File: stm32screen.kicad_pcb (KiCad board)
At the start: 4 copper layers, 46 x 46 mm, 36 parts, among them J1 SWD, J2 GC9A01, J3 OIL, J4 OIL PRESS, J5 POWER IN, J6 EGT, SW2 SW_Push, U1 TS1117BCW-3.3, U2 STM32F407VETx, U3 MAX31856

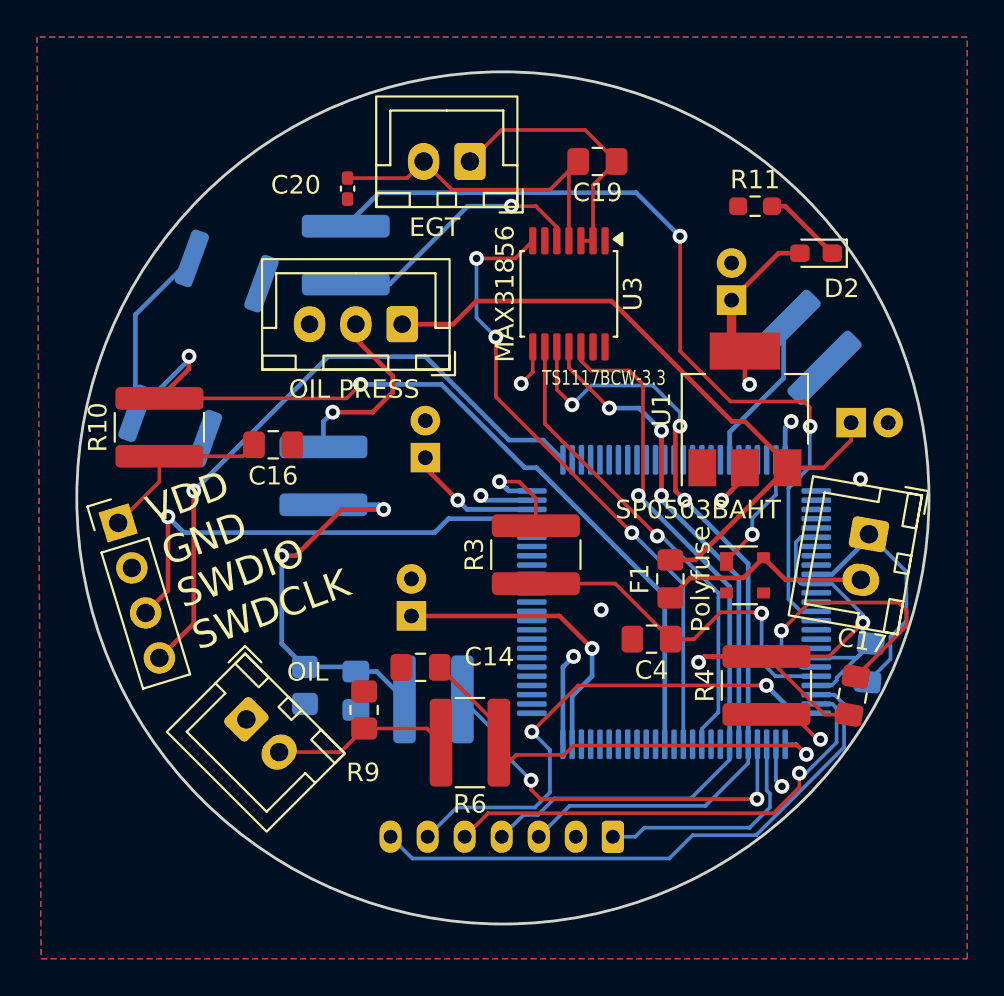
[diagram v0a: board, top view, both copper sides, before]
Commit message: Small trace changes
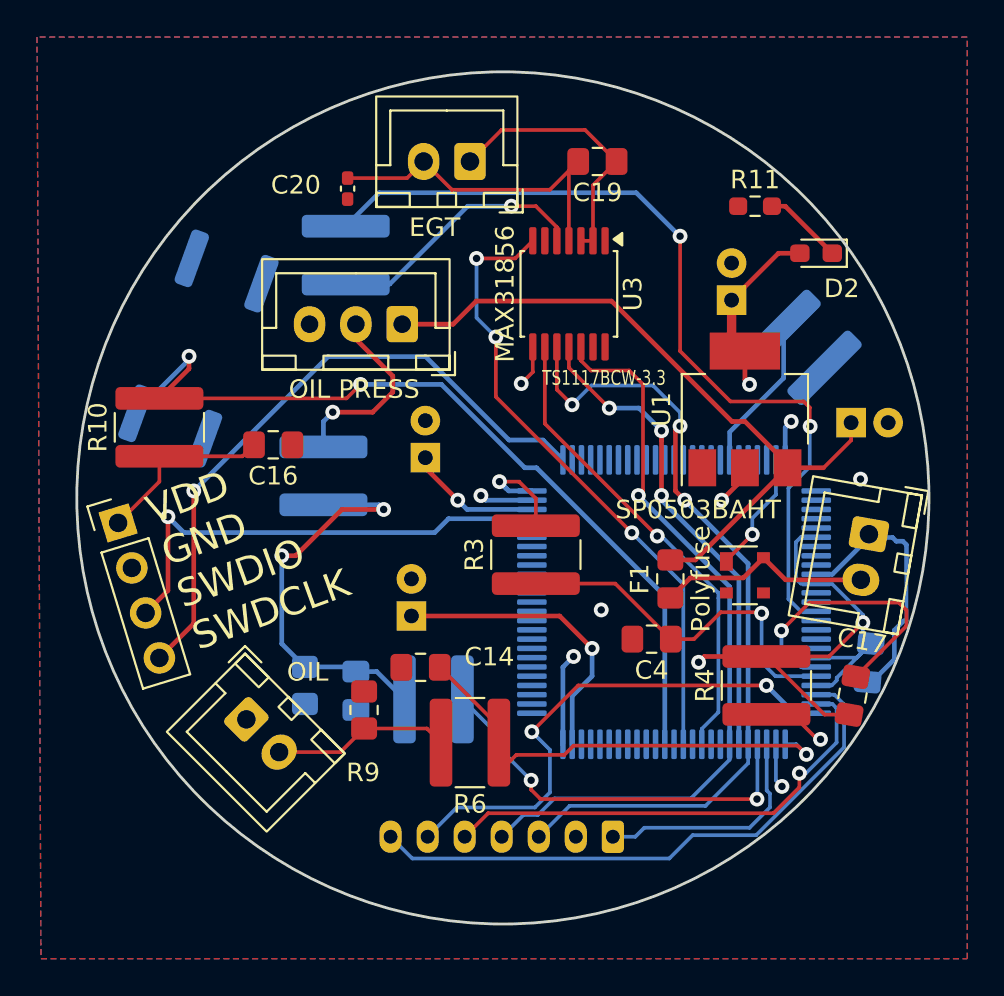
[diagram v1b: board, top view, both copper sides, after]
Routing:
- net Net-(U2-PE8): track 57.2 -> 47.5 mm
- net GND: track 41.2 -> 42.3 mm
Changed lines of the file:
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@@
 		(fp_line
 			(start -0.261252 0.734999)
-			(end 0.261251 0.734999)
+			(end 0.261251 0.734998)
 			(stroke
 				(width 0.12)
@@
 		)
 		(fp_line
-			(start -0.261251 -0.734999)
+			(start -0.261251 -0.734998)
 			(end 0.261252 -0.734999)
 			(stroke
@@
 		(tags "CK C&K SPST")
 		(property "Reference" "SW2"
-			(at -0.241564 4.279501 70)
+			(at -0.241563 4.279501 70)
 			(layer "B.SilkS")
 			(effects
@@
 		(fp_line
 			(start -0.261252 -0.735)
-			(end 0.261252 -0.734998)
+			(end 0.261252 -0.734997)
 			(stroke
 				(width 0.12)
@@
 		)
 		(fp_line
-			(start -0.261252 0.734998)
+			(start -0.261252 0.734997)
 			(end 0.261252 0.735)
 			(stroke
@@
 	)
 	(segment
-		(start 137.675 86.875)
-		(end 138 87.2)
-		(width 0.2)
+		(start 142.8496 81.5594)
+		(end 142.621 81.5594)
+		(width 0.25)
 		(layer "B.Cu")
 		(net 2)
 	)
 	(segment
-		(start 142.621 81.5594)
-		(end 143.85665 80.32375)
+		(start 137.675 86.875)
+		(end 138 87.2)
 		(width 0.2)
 		(layer "B.Cu")
@@
 	)
 	(segment
+		(start 143.9672 73.7616)
+		(end 142.869329 73.7616)
+		(width 0.25)
+		(layer "B.Cu")
+		(net 2)
+	)
+	(segment
 		(start 142.911576 81.678552)
 		(end 143.044952 81.678552)
@@
 	)
 	(segment
+		(start 142.869329 73.7616)
+		(end 142.694684 73.586955)
+		(width 0.25)
+		(layer "B.Cu")
+		(net 2)
+	)
+	(segment
+		(start 144.0688 78.7654)
+		(end 144.0688 80.3402)
+		(width 0.25)
+		(layer "B.Cu")
+		(net 2)
+	)
+	(segment
+		(start 144.719 74.1578)
+		(end 144.526 73.9648)
+		(width 0.25)
+		(layer "B.Cu")
+		(net 2)
+	)
+	(segment
+		(start 144.0688 80.3402)
+		(end 142.8496 81.5594)
+		(width 0.25)
+		(layer "B.Cu")
+		(net 2)
+	)
+	(segment
 		(start 142.694684 73.774494)
 		(end 142.694684 73.586955)
@@
 	(segment
 		(start 144.719 78.268364)
-		(end 144.719 75.611271)
-		(width 0.2)
+		(end 144.565836 78.268364)
+		(width 0.25)
 		(layer "B.Cu")
 		(net 2)
 	)
 	(segment
-		(start 143.85665 79.130714)
-		(end 144.719 78.268364)
-		(width 0.2)
+		(start 144.526 73.9648)
+		(end 144.1704 73.9648)
+		(width 0.25)
 		(layer "B.Cu")
 		(net 2)
 	)
 	(segment
-		(start 144.719 75.611271)
-		(end 142.694684 73.586955)
+		(start 144.719 78.268364)
+		(end 144.719 75.611271)
 		(width 0.2)
 		(layer "B.Cu")
@@
 	)
 	(segment
-		(start 143.85665 80.32375)
-		(end 143.85665 79.130714)
-		(width 0.2)
+		(start 144.1704 73.9648)
+		(end 143.9672 73.7616)
+		(width 0.25)
 		(layer "B.Cu")
 		(net 2)
@@
 	)
 	(segment
+		(start 144.565836 78.268364)
+		(end 144.0688 78.7654)
+		(width 0.25)
+		(layer "B.Cu")
+		(net 2)
+	)
+	(segment
 		(start 136.4 72.722709)
 		(end 136.4 73.6)
@@
 	)
 	(segment
+		(start 144.719 75.611271)
+		(end 144.719 74.1578)
+		(width 0.25)
+		(layer "B.Cu")
+		(net 2)
+	)
+	(segment
 		(start 126 78)
 		(end 118 78)
@@
 		(width 0.25)
 		(layer "B.Cu")
-		(net 20)
-	)
-	(segment
-		(start 103.099029 61.740235)
-		(end 106.143008 58.696256)
-		(width 0.25)
-		(layer "B.Cu")
-		(net 20)
-	)
-	(segment
-		(start 103.099029 67.05952)
-		(end 103.099029 61.740235)
-		(width 0.25)
-		(layer "B.Cu")

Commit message: A bit neater layout. Add missing parts to PCB. Refine silkscreen. New screenshots
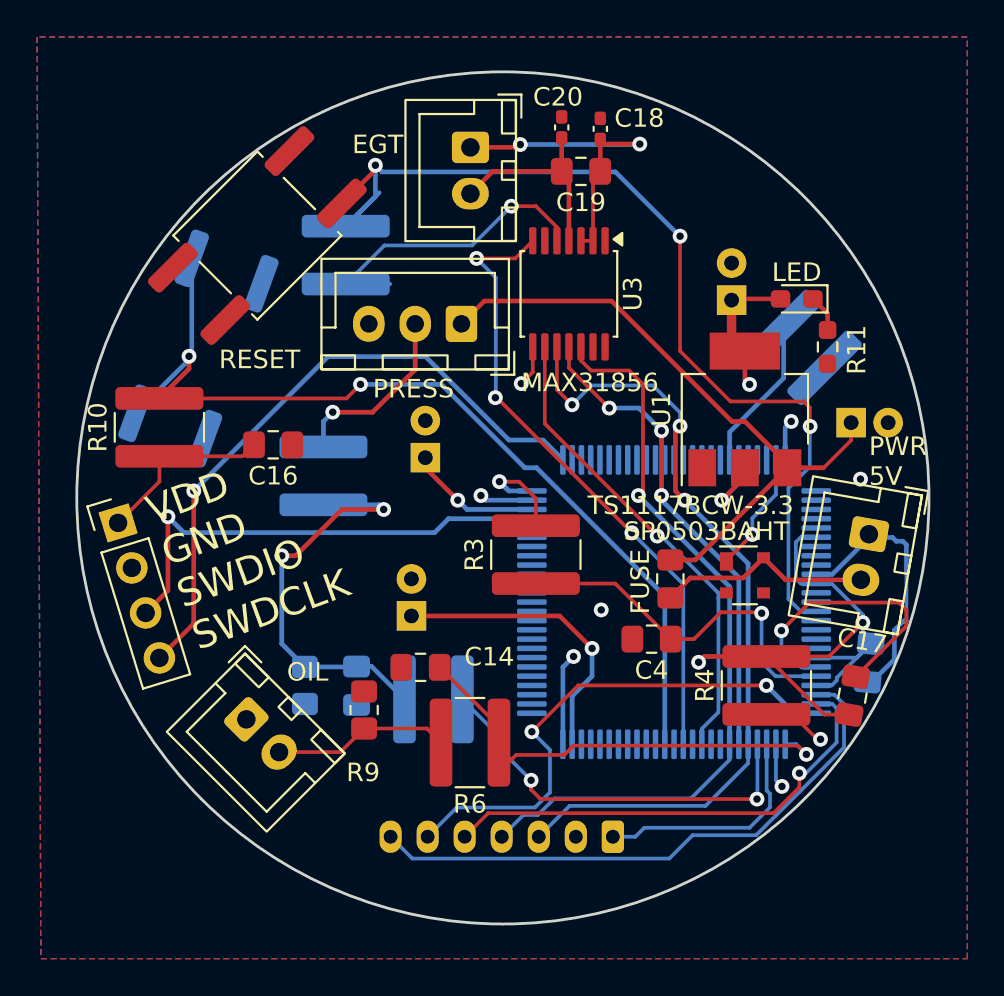
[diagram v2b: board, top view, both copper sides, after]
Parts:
- added C18: 0.01uF, Capacitor_SMD:C_0402_1005Metric_Pad0.74x0.62mm_HandSolder, F.Cu at (128.2, 51.7)
- added RESET: SW_Push, Button_Switch_SMD:SW_Push_1P1T_NO_CK_KSC9xxG, F.Cu at (109.7, 57.5)
- F1: value Polyfuse -> FUSE
- J4: value OIL PRESS -> PRESS
- moved C20 12.0 mm to (126.1, 51.6), turned to 90 degrees
- moved R11 8.55 mm to (140.5, 63.5), turned to 90 degrees
- moved J4 3.20 mm to (120.7, 62.2)
- moved D2 2.68 mm to (138.8, 60.9)
- moved C19 1.04 mm to (127.1, 54.0)
- moved J6 0.76 mm to (121.2, 52.7), turned to -90 degrees
- moved C15 0.27 mm to (115.0, 81.8)
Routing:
- net NRST: track 46.8 -> 54.3 mm, vias 2 -> 3
- net Net-(J6-Pin_2): track 18.6 -> 11.1 mm
- net Net-(U2-PE8): track 47.5 -> 52.9 mm
- net Vin: track 38.5 -> 35.3 mm
- net Net-(J6-Pin_1): track 14.8 -> 17.7 mm, vias 0 -> 2
- net Net-(D2-K): track 4.31 -> 2.01 mm
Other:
- board text added: "PWR 5V"

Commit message: THT caps to MLCC as per TS1117B datasheet. STM32 ref caps as well
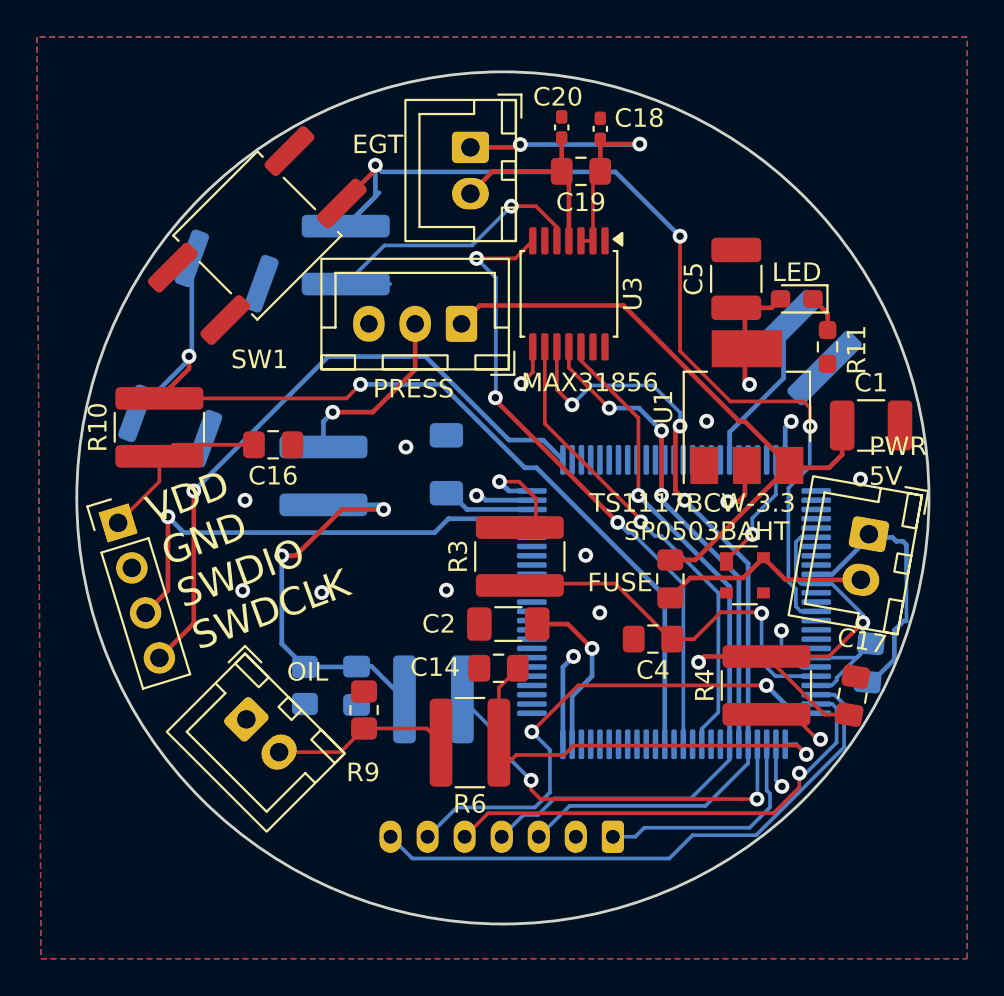
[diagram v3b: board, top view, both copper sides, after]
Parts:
- C1: footprint Capacitor_THT:CP_Radial_D5.0mm_P2.00mm -> Capacitor_SMD:C_1210_3225Metric_Pad1.33x2.70mm_HandSolder; moved to F.Cu
- C2: footprint Capacitor_THT:CP_Radial_D5.0mm_P2.00mm -> Capacitor_SMD:C_1206_3216Metric_Pad1.33x1.80mm_HandSolder; moved to F.Cu
- C3: footprint Capacitor_THT:CP_Radial_D5.0mm_P2.00mm -> Capacitor_SMD:C_1206_3216Metric_Pad1.33x1.80mm_HandSolder
- C5: value 10uF -> 100uF; footprint Capacitor_THT:CP_Radial_D5.0mm_P2.00mm -> Capacitor_SMD:C_1210_3225Metric_Pad1.33x2.70mm_HandSolder; moved to F.Cu
- moved C2 5.25 mm to (123.2, 78.4), turned to 180 degrees
- moved C14 4.21 mm to (122.7, 80.8)
- moved C3 1.19 mm to (119.9, 69.8)
- moved C5 1.17 mm to (135.5, 59.8)
- moved C1 1.09 mm to (142.8, 67.7)
- moved R3 0.87 mm to (123.9, 74.8)
- moved U1 0.16 mm to (136.1, 66.7)
- moved C4 0.07 mm to (131.0, 79.2)
- renumbered RESET to SW1
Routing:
- net GND: track 42.3 -> 30.0 mm, vias 6 -> 13
- net Net-(U2-VCAP_1): track 16.1 -> 9.12 mm
- net Net-(U2-VCAP_2): track 7.23 -> 4.21 mm, vias 1 -> 0
- net SDI: track 41.0 -> 39.6 mm
- net VDD: track 100.7 -> 101.9 mm
- net Net-(U2-PA3): track 25.2 -> 24.2 mm

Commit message: Adjusted silkscreen and component layout, changed some component values so that silkscreen doesn't change every time
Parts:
- SW1: value SW_Push -> NRST
- SW2: value SW_Push -> USER
- moved C1 1.00 mm to (142.6, 66.8)
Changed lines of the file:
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@@
 	(footprint "Capacitor_SMD:C_1210_3225Metric_Pad1.33x2.70mm_HandSolder"
 		(layer "F.Cu")
-		(at 142.8111 67.7164)
+		(at 142.5571 66.7512)
 		(descr "Capacitor SMD 1210 (3225 Metric), square (rectangular) end terminal, IPC-7351 nominal with elongated pad for handsoldering. (Body size source: IPC-SM-782 page 76, https://www.pcb-3d.com/wordpress/wp-content/uploads/ipc-sm-782a_amendment_1_and_2.pdf), generated with kicad-footprint-generator")
 		(tags "capacitor handsolder")
@@
 			(at -4.647566 4.8198 0)
 			(layer "F.SilkS")
+			(hide yes)
 			(effects
 				(font
@@
 			)
 		)
-		(property "Value" "SW_Push"
-			(at 0 -4.23 45)
-			(layer "F.Fab")
+		(property "Value" "NRST"
+			(at -3.480133 4.191182 45)
+			(layer "F.SilkS")
 			(effects
 				(font
@@
 		(tags "resistor handsolder")
 		(property "Reference" "R11"
-			(at -0.1543 1.5748 270)
+			(at 0.8909 2.1844 0)
 			(layer "F.SilkS")
 			(effects
@@
 		(tags "resistor handsolder")
 		(property "Reference" "R5"
-			(at -3.0125 3.32 0)
+			(at 0.0107 3.3536 0)
 			(layer "B.SilkS")
 			(effects
@@
 		(tags "resistor handsolder")
 		(property "Reference" "R7"
-			(at 2.794 -0.254 0)
+			(at -2.502 -0.018 0)
 			(layer "B.SilkS")
 			(effects
@@
 		(tags "capacitor handsolder")
 		(property "Reference" "C15"
-			(at 4.4495 1.3858 180)
+			(at -2.6201 0.0254 180)
 			(layer "B.SilkS")
 			(effects
@@
 			(at -0.241563 4.279501 70)
 			(layer "B.SilkS")
+			(hide yes)
 			(effects
 				(font
@@
 			)
 		)
-		(property "Value" "SW_Push"
+		(property "Value" "USER"
 			(at 0 4.23 70)
-			(layer "B.Fab")
+			(layer "B.SilkS")
 			(effects
 				(font

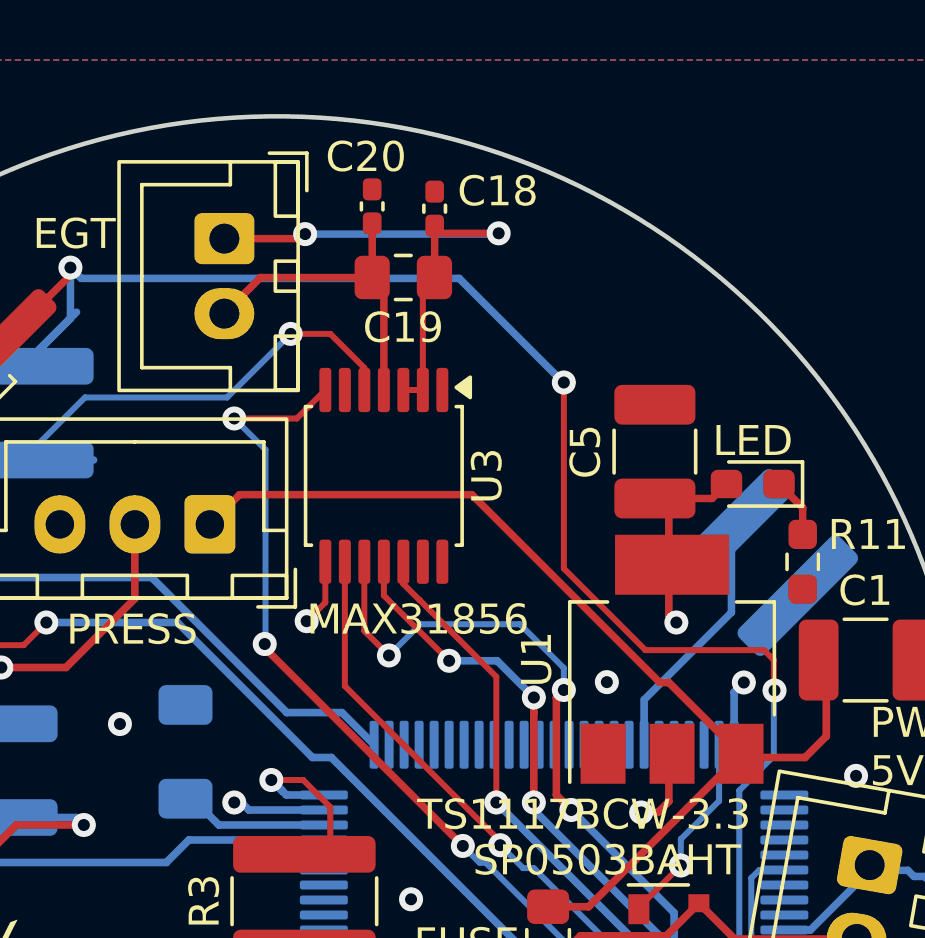
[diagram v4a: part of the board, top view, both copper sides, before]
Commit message: Changed footprints to larger ones and for general unity of footprints
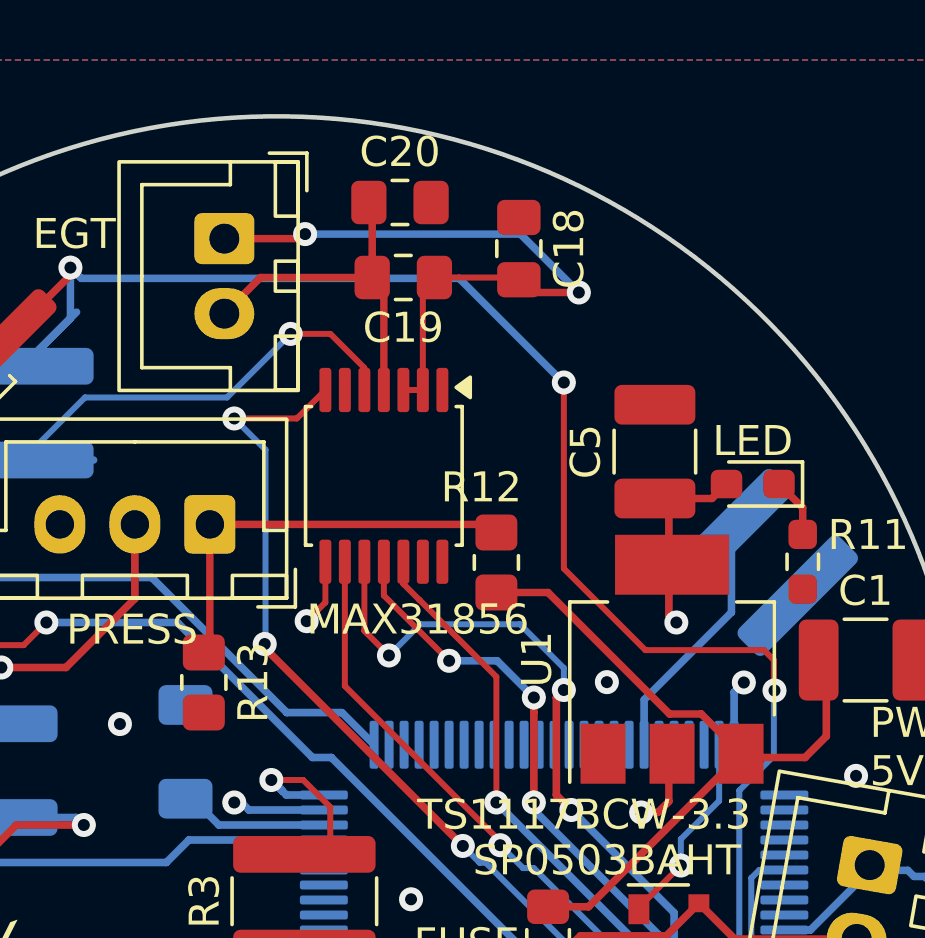
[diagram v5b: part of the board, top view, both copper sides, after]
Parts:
- added R12: 4.7k, Resistor_SMD:R_0805_2012Metric_Pad1.20x1.40mm_HandSolder, F.Cu at (130.2, 63.5)
- added R13: 3.3k, Resistor_SMD:R_0805_2012Metric_Pad1.20x1.40mm_HandSolder, F.Cu at (120.5, 67.5)
- C18, C20: value 0.01uF -> 10nF; footprint Capacitor_SMD:C_0402_1005Metric_Pad0.74x0.62mm_HandSolder -> Capacitor_SMD:C_0805_2012Metric_Pad1.18x1.45mm_HandSolder
- R11: value 68 -> 160
- moved C18 3.11 mm to (131.0, 53.0)
- moved C20 0.94 mm to (127.0, 51.5), turned to 0 degrees
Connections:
- J4 pad 1: Vin -> 5V
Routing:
- net 5V: track 0.00 -> 14.0 mm
- net Vin: track 35.0 -> 23.8 mm
- net Net-(J6-Pin_1): track 17.7 -> 22.3 mm
- net Net-(J6-Pin_2): track 11.1 -> 11.9 mm

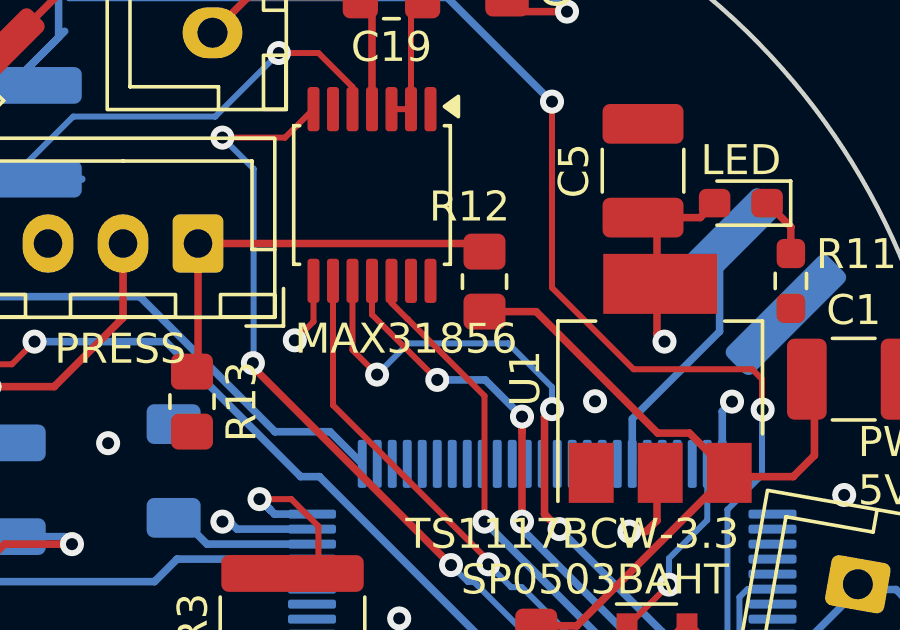
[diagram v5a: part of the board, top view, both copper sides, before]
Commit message: Fix missing ground connection for MAX31856
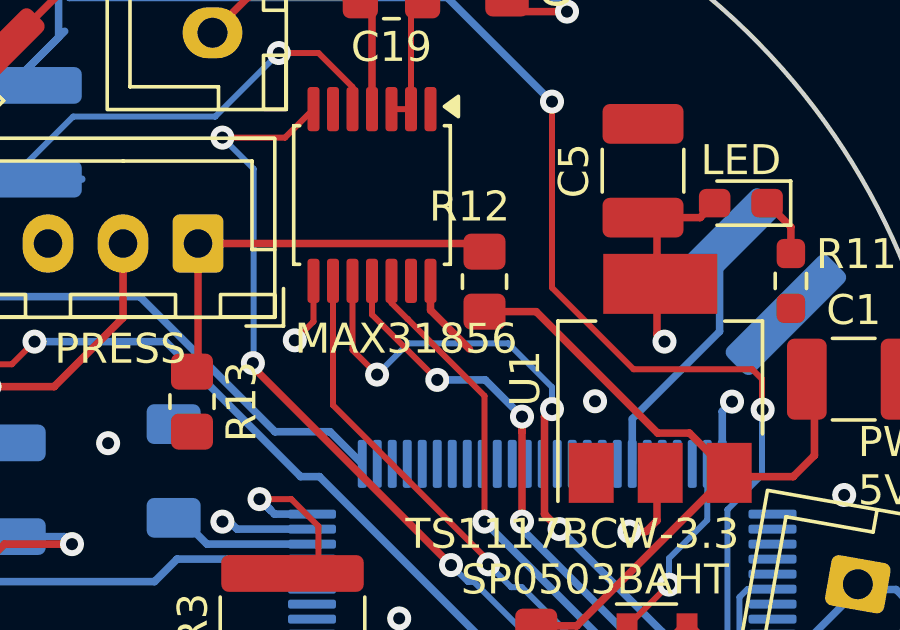
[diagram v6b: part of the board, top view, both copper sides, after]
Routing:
- net GND: track 30.0 -> 32.8 mm
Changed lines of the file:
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@@
+	)
+	(segment
+		(start 128.45 63.475)
+		(end 128.45 64.45)
+		(width 0.25)
+		(layer "F.Cu")
+		(net 2)
 	)
 	(segment
@@
 		(layer "F.Cu")
 		(net 2)
+	)
+	(segment
+		(start 128.45 64.45)
+		(end 129.75 65.75)
+		(width 0.25)
+		(layer "F.Cu")
+		(net 2)
